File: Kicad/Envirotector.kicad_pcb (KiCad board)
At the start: 2 copper layers, 75 x 77.7 mm, 11 parts, among them J1 OLED Display, J2 Micro_SD_Card, SW1 RotaryEncoder_Switch, U1 XIAO-RP2040-DIP, U2 DHT11

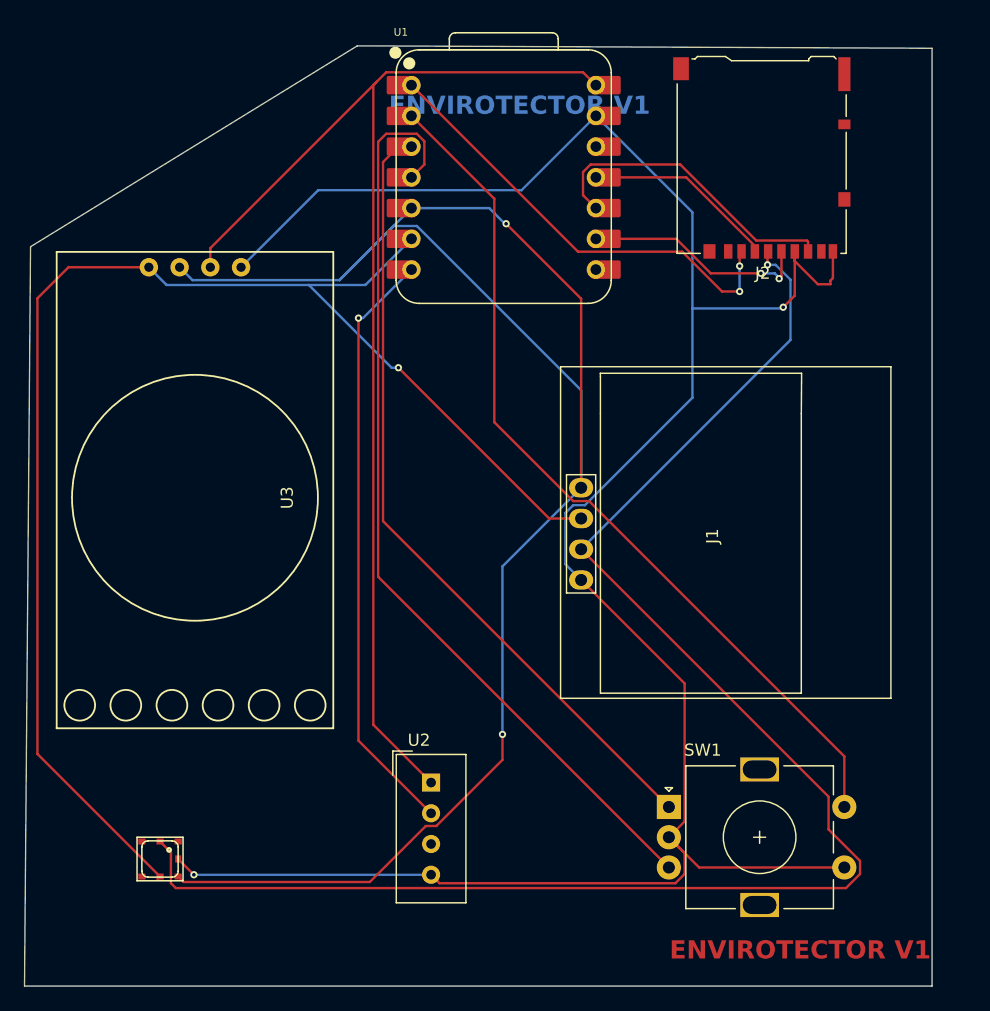
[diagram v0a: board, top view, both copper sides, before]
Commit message: updated footprint and case for bmp180 breakout board
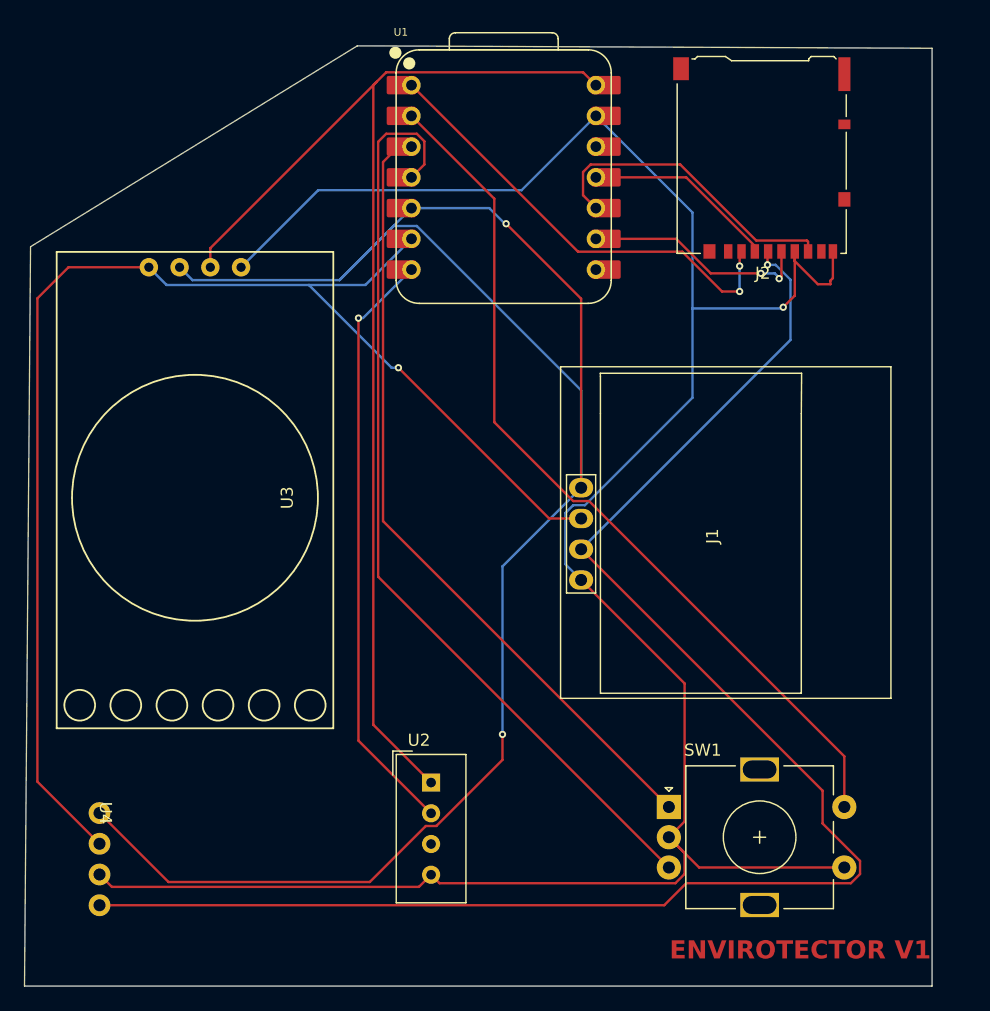
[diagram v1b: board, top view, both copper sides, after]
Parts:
- U4: footprint SPARK:BMP180 -> SPARK:Untitled
- moved U4 6.28 mm to (76.2, 120.7), turned to -90 degrees
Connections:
- U4 pad 1: (no net) -> +3.3V
- U4 pad 2: +3.3V -> GND
- U4 pad 3: (no net) -> Net-(J1-Pin_2)
- U4 pad 4: (no net) -> Net-(J1-Pin_1)
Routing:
- net Net-(J1-Pin_1): track 146.7 -> 155.3 mm
- net GND: track 189.0 -> 195.8 mm, vias 2 -> 1
- net Net-(J1-Pin_2): track 117.5 -> 112.5 mm
- net +3.3V: track 130.8 -> 133.3 mm

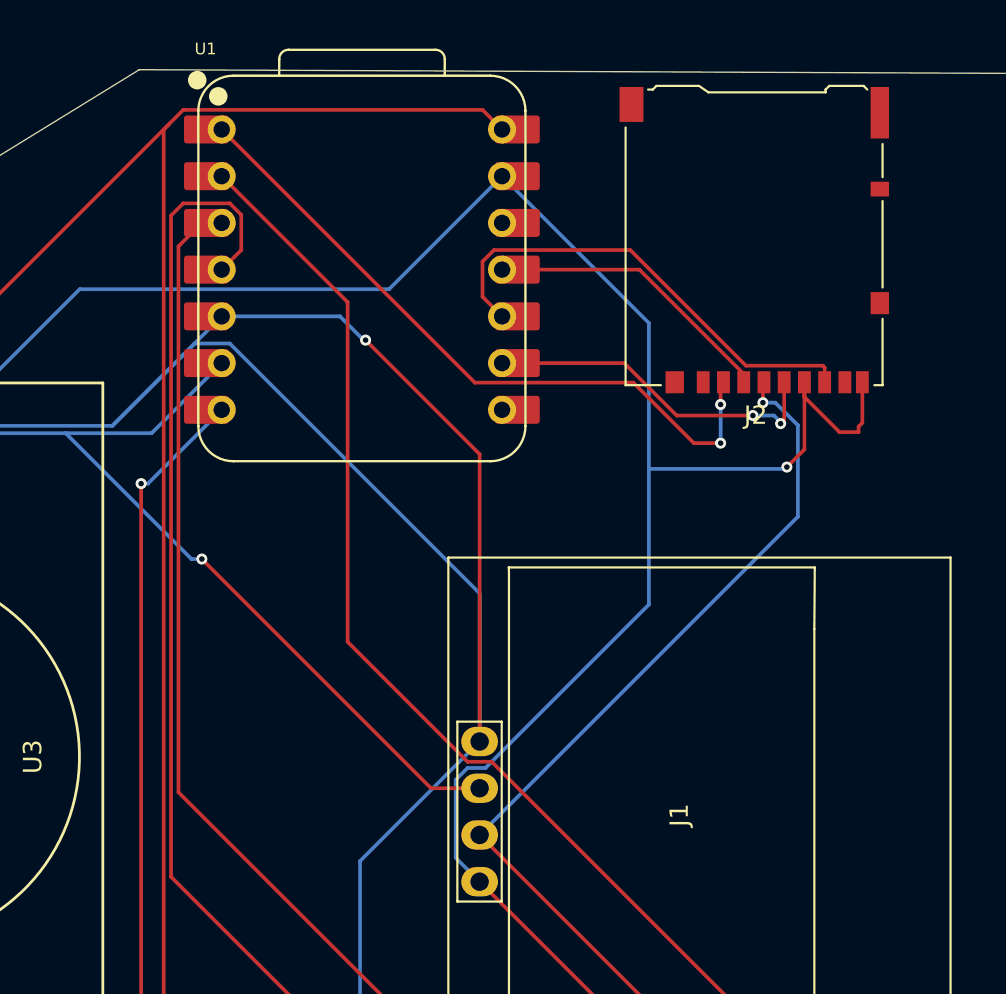
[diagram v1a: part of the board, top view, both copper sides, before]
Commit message: updated the sd card reader to breakoutboard
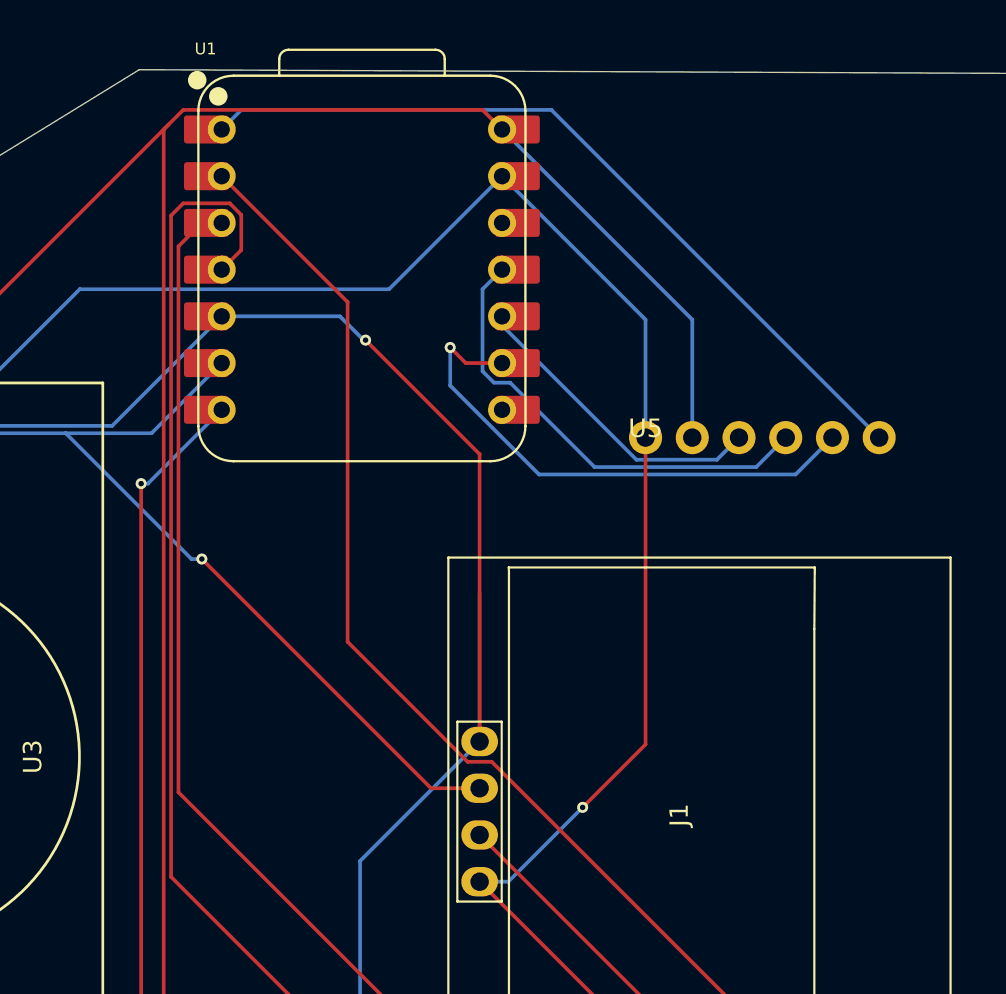
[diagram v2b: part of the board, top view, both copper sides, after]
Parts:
- removed J2: Micro_SD_Card, Connector_Card:microSD_HC_Hirose_DM3AT-SF-PEJM5
- added U5: ~, SDReader:Untitled, F.Cu at (125.0, 77.3)
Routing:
- net +3.3V: track 133.3 -> 100.3 mm, vias 1 -> 0
- net Net-(J1-Pin_1): track 155.3 -> 127.9 mm
- net +5V: track 99.9 -> 120.9 mm
- net GND: track 195.8 -> 175.0 mm
- net Net-(U1-GPIO2/SCK): track 18.9 -> 28.9 mm, vias 2 -> 1
- net Net-(U1-GPIO3/MOSI): track 15.9 -> 25.3 mm
- net Net-(U1-GPIO4/MISO): track 25.7 -> 16.9 mm
- net Net-(U1-GPIO26/ADC0/A0): track 37.6 -> 43.6 mm, vias 2 -> 0

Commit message: updated 3.3v xiao output
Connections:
- U1 pad 12: unconnected-(U1-3V3-Pad12) -> +3.3V
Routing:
- net +3.3V: track 100.3 -> 139.1 mm, vias 0 -> 1
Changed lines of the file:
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@@
 	(net 7 "Net-(U1-GPIO29{slash}ADC3{slash}A3)")
 	(net 8 "Net-(U1-GPIO0{slash}TX)")
-	(net 9 "unconnected-(U1-3V3-Pad12)")
-	(net 10 "+5V")
-	(net 11 "unconnected-(U1-GPIO1{slash}RX-Pad8)")
-	(net 12 "unconnected-(U2-NC-Pad3)")
-	(net 13 "Net-(U1-GPIO2{slash}SCK)")
-	(net 14 "Net-(U1-GPIO26{slash}ADC0{slash}A0)")
-	(net 15 "Net-(U1-GPIO3{slash}MOSI)")
-	(net 16 "Net-(U1-GPIO4{slash}MISO)")
+	(net 9 "+5V")
+	(net 10 "unconnected-(U1-GPIO1{slash}RX-Pad8)")
+	(net 11 "unconnected-(U2-NC-Pad3)")
+	(net 12 "Net-(U1-GPIO2{slash}SCK)")
+	(net 13 "Net-(U1-GPIO26{slash}ADC0{slash}A0)")
+	(net 14 "Net-(U1-GPIO3{slash}MOSI)")
+	(net 15 "Net-(U1-GPIO4{slash}MISO)")
 	(footprint "Sensor:Aosong_DHT11_5.5x12.0_P2.54mm"
 		(layer "F.Cu")
@@
 			(layers "*.Cu" "*.Mask")
 			(remove_unused_layers no)
-			(net 10 "+5V")
+			(net 9 "+5V")
 			(pinfunction "VDD")
 			(pintype "power_in")
@@
 			(layers "*.Cu" "*.Mask")
 			(remove_unused_layers no)
-			(net 12 "unconnected-(U2-NC-Pad3)")
+			(net 11 "unconnected-(U2-NC-Pad3)")
 			(pinfunction "NC")
 			(pintype "no_connect")
@@
 			(layers "*.Cu" "*.Mask")
 			(remove_unused_layers no)
-			(net 10 "+5V")
+			(net 9 "+5V")
 			(pinfunction "VCC")
 			(pintype "power_in")
@@
 			(layers "*.Cu" "*.Mask")
 			(remove_unused_layers no)
-			(net 16 "Net-(U1-GPIO4{slash}MISO)")
+			(net 15 "Net-(U1-GPIO4{slash}MISO)")
 			(pinfunction "MISO")
 			(pintype "input")
@@
 			(layers "*.Cu" "*.Mask")
 			(remove_unused_layers no)
-			(net 15 "Net-(U1-GPIO3{slash}MOSI)")
+			(net 14 "Net-(U1-GPIO3{slash}MOSI)")
 			(pinfunction "MOSI")
 			(pintype "output")
@@
 			(layers "*.Cu" "*.Mask")
 			(remove_unused_layers no)
-			(net 13 "Net-(U1-GPIO2{slash}SCK)")
+			(net 12 "Net-(U1-GPIO2{slash}SCK)")
 			(pinfunction "SCK")
 			(pintype "output")
@@
 			(layers "*.Cu" "*.Mask")
 			(remove_unused_layers no)
-			(net 14 "Net-(U1-GPIO26{slash}ADC0{slash}A0)")
+			(net 13 "Net-(U1-GPIO26{slash}ADC0{slash}A0)")
 			(pinfunction "CS")
 			(pintype "output")
@@
 			(layers "*.Cu" "*.Mask")
 			(remove_unused_layers no)
-			(net 10 "+5V")
+			(net 9 "+5V")
 			(pinfunction "VCC")
 			(pintype "input")
@@
 			(layers "F.Cu" "F.Mask")
 			(roundrect_rratio 0.1)
-			(net 14 "Net-(U1-GPIO26{slash}ADC0{slash}A0)")
+			(net 13 "Net-(U1-GPIO26{slash}ADC0{slash}A0)")
 			(pinfunction "GPIO26/ADC0/A0")
 			(pintype "passive")
@@
 			(layers "*.Cu" "*.Mask")
 			(remove_unused_layers no)
-			(net 14 "Net-(U1-GPIO26{slash}ADC0{slash}A0)")
+			(net 13 "Net-(U1-GPIO26{slash}ADC0{slash}A0)")
 			(pinfunction "GPIO26/ADC0/A0")
 			(pintype "passive")
@@
 			(layers "*.Cu" "*.Mask")
 			(remove_unused_layers no)
-			(net 11 "unconnected-(U1-GPIO1{slash}RX-Pad8)")
+			(net 10 "unconnected-(U1-GPIO1{slash}RX-Pad8)")
 			(pinfunction "GPIO1/RX")
 			(pintype "passive")
@@
 			(layers "F.Cu" "F.Mask")
 			(roundrect_rratio 0.1)
-			(net 11 "unconnected-(U1-GPIO1{slash}RX-Pad8)")
+			(net 10 "unconnected-(U1-GPIO1{slash}RX-Pad8)")
 			(pinfunction "GPIO1/RX")
 			(pintype "passive")
@@
 			(layers "*.Cu" "*.Mask")
 			(remove_unused_layers no)
-			(net 13 "Net-(U1-GPIO2{slash}SCK)")
+			(net 12 "Net-(U1-GPIO2{slash}SCK)")
 			(pinfunction "GPIO2/SCK")
 			(pintype "passive")
@@
 			(layers "F.Cu" "F.Mask")
 			(roundrect_rratio 0.1)
-			(net 13 "Net-(U1-GPIO2{slash}SCK)")
+			(net 12 "Net-(U1-GPIO2{slash}SCK)")
 			(pinfunction "GPIO2/SCK")
 			(pintype "passive")
@@
 			(layers "*.Cu" "*.Mask")
 			(remove_unused_layers no)
-			(net 16 "Net-(U1-GPIO4{slash}MISO)")
+			(net 15 "Net-(U1-GPIO4{slash}MISO)")
 			(pinfunction "GPIO4/MISO")
 			(pintype "passive")
@@
 			(layers "F.Cu" "F.Mask")
 			(roundrect_rratio 0.1)
-			(net 16 "Net-(U1-GPIO4{slash}MISO)")
+			(net 15 "Net-(U1-GPIO4{slash}MISO)")
 			(pinfunction "GPIO4/MISO")
 			(pintype "passive")
@@
 			(layers "*.Cu" "*.Mask")
 			(remove_unused_layers no)
-			(net 15 "Net-(U1-GPIO3{slash}MOSI)")
+			(net 14 "Net-(U1-GPIO3{slash}MOSI)")
 			(pinfunction "GPIO3/MOSI")
 			(pintype "passive")
@@
 			(layers "F.Cu" "F.Mask")
 			(roundrect_rratio 0.1)
-			(net 15 "Net-(U1-GPIO3{slash}MOSI)")
+			(net 14 "Net-(U1-GPIO3{slash}MOSI)")
 			(pinfunction "GPIO3/MOSI")
 			(pintype "passive")
@@
 			(layers "*.Cu" "*.Mask")
 			(remove_unused_layers no)
-			(net 9 "unconnected-(U1-3V3-Pad12)")
+			(net 3 "+3.3V")
 			(pinfunction "3V3")
 			(pintype "passive")
@@
 			(layers "F.Cu" "F.Mask")
 			(roundrect_rratio 0.1)
-			(net 9 "unconnected-(U1-3V3-Pad12)")
+			(net 3 "+3.3V")
 			(pinfunction "3V3")
 			(pintype "passive")
@@
 			(layers "*.Cu" "*.Mask")
 			(remove_unused_layers no)
-			(net 10 "+5V")
+			(net 9 "+5V")
 			(pinfunction "VBUS")
 			(pintype "passive")
@@
 			(layers "F.Cu" "F.Mask")
 			(roundrect_rratio 0.1)
-			(net 10 "+5V")
+			(net 9 "+5V")
 			(pinfunction "VBUS")
 			(pintype "passive")
@@
 	)
 	(segment
+		(start 113.799 69.0495)
+		(end 113.799 75.4319)
+		(width 0.2)
+		(layer "F.Cu")
+		(net 3)
+	)
+	(segment
 		(start 135.954992 118.854992)
 		(end 116 98.9)
@@
 	)
 	(segment
+		(start 119.3 80.9329)
+		(end 119.3 96.3)
+		(width 0.2)
+		(layer "F.Cu")
+		(net 3)
+	)
+	(segment
 		(start 76.2 128.32)
 		(end 122.8649 128.32)
@@
 	)
 	(segment
+		(start 117.22 65.6285)
+		(end 113.799 69.0495)
+		(width 0.2)
+		(layer "F.Cu")
+		(net 3)
+	)
+	(segment
 		(start 135.954992 121.5651)
 		(end 135.954992 118.854992)
@@
 	)
 	(segment
+		(start 113.799 75.4319)
+		(end 119.3 80.9329)
+		(width 0.2)
+		(layer "F.Cu")
+		(net 3)
+	)
+	(segment
 		(start 124.6839 126.501)
 		(end 138.288892 126.501)
@@
 		(net 3)
 	)
+	(via
+		(at 119.3 96.3)
+		(size 0.6)
+		(drill 0.3)
+		(layers "F.Cu" "B.Cu")
+		(net 3)
+	)
+	(segment
+		(start 116.7 98.9)
+		(end 116 98.9)
+		(width 0.2)
+		(layer "B.Cu")
+		(net 3)
+	)
+	(segment
+		(start 119.3 96.3)
+		(end 116.7 98.9)
+		(width 0.2)
+		(layer "B.Cu")
+		(net 3)
+	)
 	(segment
 		(start 123.25 122.7)
@@
 		(width 0.2)
 		(layer "F.Cu")
-		(net 10)
+		(net 9)
 	)
 	(segment
@@
 		(width 0.2)
 		(layer "F.Cu")
-		(net 10)
+		(net 9)
 	)
 	(segment
@@
 		(width 0.2)
 		(layer "F.Cu")
-		(net 10)
+		(net 9)
 	)
 	(segment
@@
 		(width 0.2)
 		(layer "F.Cu")
-		(net 10)
+		(net 9)
 	)
 	(segment
@@
 		(width 0.2)
 		(layer "F.Cu")
-		(net 10)
+		(net 9)
 	)
 	(segment
@@
 		(width 0.2)
 		(layer "F.Cu")
-		(net 10)
+		(net 9)
 	)
 	(segment
@@
 		(width 0.2)
 		(layer "F.Cu")
-		(net 10)
+		(net 9)
 	)
 	(segment
@@
 		(width 0.2)
 		(layer "F.Cu")
-		(net 10)
+		(net 9)
 	)
 	(segment
@@
 		(width 0.2)
 		(layer "B.Cu")
-		(net 10)
+		(net 9)
 	)
 	(segment
@@
 		(width 0.2)
 		(layer "B.Cu")
-		(net 10)
+		(net 9)
 	)
 	(segment
@@
 		(width 0.2)
 		(layer "F.Cu")
-		(net 13)
+		(net 12)
 	)
 	(segment
@@
 		(width 0.2)
 		(layer "F.Cu")
-		(net 13)
+		(net 12)
 	)
 	(via
@@
 		(drill 0.3)
 		(layers "F.Cu" "B.Cu")
-		(net 13)
+		(net 12)
 	)
 	(segment
@@
 		(width 0.2)
 		(layer "B.Cu")
-		(net 13)
+		(net 12)
 	)
 	(segment
@@
 		(width 0.2)
 		(layer "B.Cu")
-		(net 13)
+		(net 12)
 	)
 	(segment
@@
 		(width 0.2)
 		(layer "B.Cu")
-		(net 13)
+		(net 12)
 	)
 	(segment
@@
 		(width 0.2)
 		(layer "B.Cu")
-		(net 13)
+		(net 12)
 	)
 	(segment
@@
 		(width 0.2)
 		(layer "B.Cu")
-		(net 14)
+		(net 13)
 	)
 	(segment
@@
 		(width 0.2)
 		(layer "B.Cu")
-		(net 14)
+		(net 13)
 	)
 	(segment
@@
 		(width 0.2)
 		(layer "B.Cu")
-		(net 14)
+		(net 13)
 	)
 	(segment
@@
 		(width 0.2)
 		(layer "B.Cu")
-		(net 15)
+		(net 14)
 	)
 	(segment
@@
 		(width 0.2)
 		(layer "B.Cu")
-		(net 15)
+		(net 14)
 	)
 	(segment
@@
 		(width 0.2)
 		(layer "B.Cu")
-		(net 15)
+		(net 14)
 	)
 	(segment
@@
 		(width 0.2)
 		(layer "B.Cu")
-		(net 15)
+		(net 14)
 	)
 	(segment
@@
 		(width 0.2)
 		(layer "B.Cu")
-		(net 15)
+		(net 14)
 	)
 	(segment
@@
 		(width 0.2)
 		(layer "B.Cu")
-		(net 15)
+		(net 14)
 	)
 	(segment
@@
 		(width 0.2)
 		(layer "B.Cu")
-		(net 15)
+		(net 14)
 	)
 	(segment
@@
 		(width 0.2)
 		(layer "B.Cu")
-		(net 16)
+		(net 15)
 	)
 	(segment
@@
 		(width 0.2)
 		(layer "B.Cu")
-		(net 16)
+		(net 15)
 	)
 	(segment
@@
 		(width 0.2)
 		(layer "B.Cu")
-		(net 16)
+		(net 15)
 	)
 	(segment
@@
 		(width 0.2)
 		(layer "B.Cu")
-		(net 16)
+		(net 15)
 	)
 	(embedded_fonts no)
